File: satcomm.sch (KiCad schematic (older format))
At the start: 15 parts

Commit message: circuit extended
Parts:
- added C6: 10u TANT, symbol C
- added C7: 22u TANT, symbol C
- added R5: 121, symbol R
- added R6: 169, symbol R
- added U2: LM1117, symbol LM1117
- gave numbers to parts that had none: 15
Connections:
- net +5V: now also C6.1, U2.3 (VIN)
- net GND: now also C6.2, C7.2, R6.2
- new net +3V: C7.1, R5.1, R5.2, R6.1, U2.1 (ADJ/GND), U2.2 (VOUT)
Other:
- note added: "battery input / boost converter for 5V"
- note added: "linear voltage regulator for 3V\n"
- note added: "low pass / supercap buffer for 5V"
- moved on the sheet: BT1, C1, C2, C3, C4, C5, D1, L1, L2, R1, R2, R3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

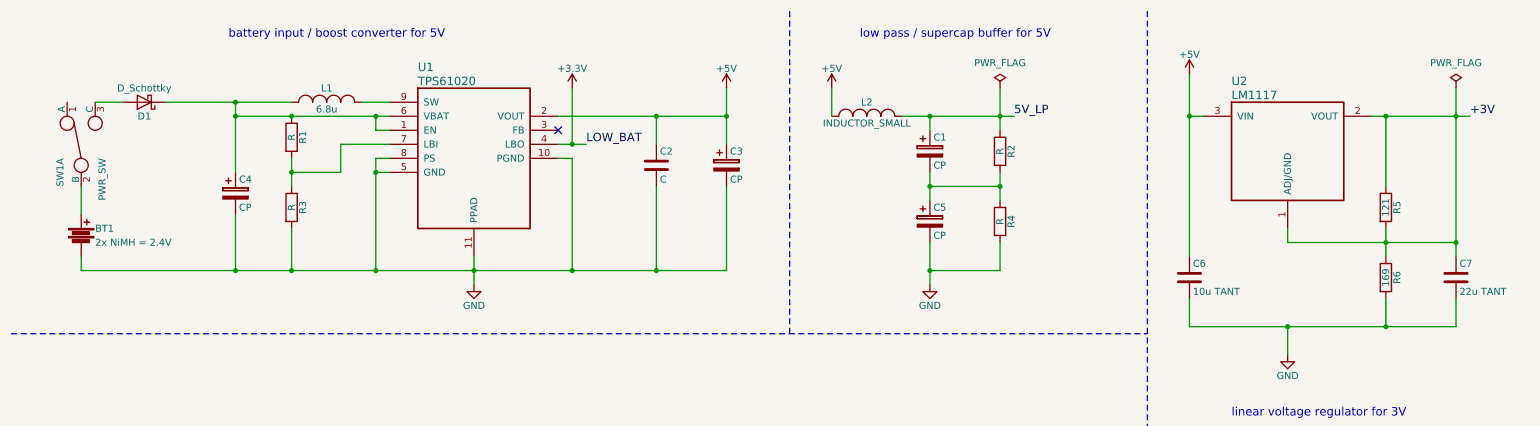
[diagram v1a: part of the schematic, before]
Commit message: added some zero ohm resistors for current measure
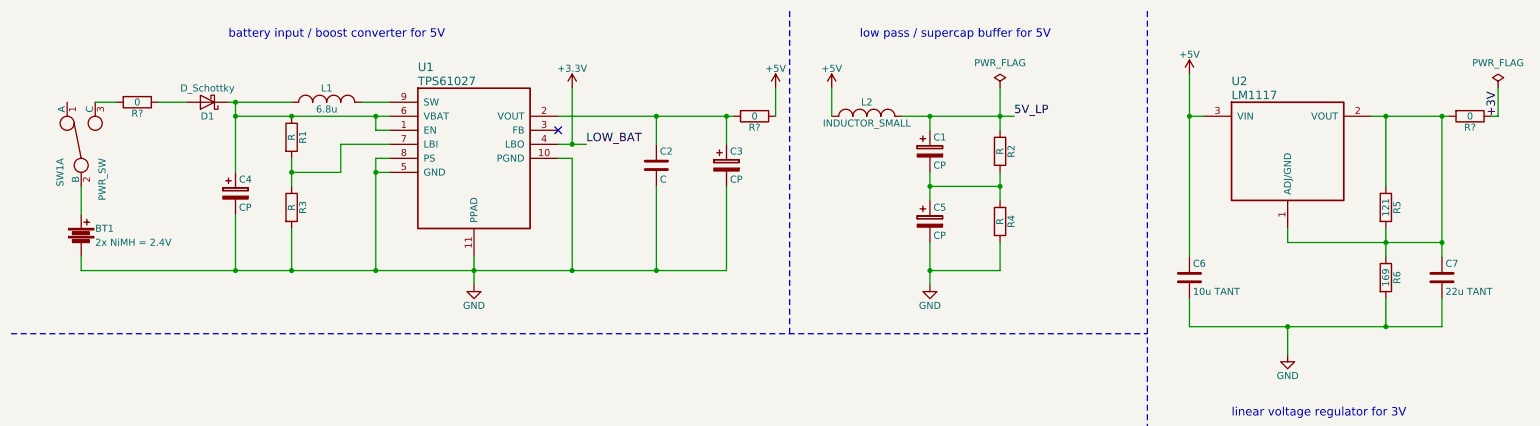
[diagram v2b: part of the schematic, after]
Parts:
- added R? (x3): 0, symbol R
- U1: value TPS61020 -> TPS61027
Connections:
- net +3V: now also R?.1; no longer C7.1, R5.1, R5.2, R6.1, U2.1 (ADJ/GND), U2.2 (VOUT)
- net +5V: now also R?.1; no longer C2.1, C3.1, U1.2 (VOUT)
- net at SW1.3 (C): now also R?.2; no longer D1.2 (A)
- new net: C2.1, C3.1, R?.2, U1.2 (VOUT)
- new net: D1.2 (A), R?.1
- new net: C7.1, R5.1, R5.2, R6.1, R?.2, U2.1 (ADJ/GND), U2.2 (VOUT)
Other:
- moved on the sheet: C7, D1
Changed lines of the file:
@@
 P 3150 1100
 F 0 "U1" H 3350 1350 60  0000 L CNN
-F 1 "TPS61020" H 3350 1250 60  0000 L CNN
+F 1 "TPS61027" H 3350 1250 60  0000 L CNN
 F 2 "" H 3150 1100 60  0000 C CNN
 F 3 "" H 3150 1100 60  0000 C CNN
@@
 	3150 1300 3050 1300
 Wire Wire Line
-	3050 1300 3050 1200
+	3050 1200 3050 1300
 Wire Wire Line
 	2050 1200 3150 1200
@@
 	2450 1500 2450 1700
 Wire Wire Line
-	2450 2000 2450 2300
+	2450 2300 2450 2000
 Connection ~ 3050 1200
 Connection ~ 3050 2300
@@
 L D_Schottky D1
 U 1 1 58D016A7
-P 1400 1100
-F 0 "D1" H 1400 1200 50  0000 C CNN
-F 1 "D_Schottky" H 1400 1000 50  0000 C CNN
-F 2 "" H 1400 1100 50  0000 C CNN
-F 3 "" H 1400 1100 50  0000 C CNN
-	1    1400 1100
+P 1850 1100
+F 0 "D1" H 1850 1200 50  0000 C CNN
+F 1 "D_Schottky" H 1850 1000 50  0000 C CNN
+F 2 "" H 1850 1100 50  0000 C CNN
+F 3 "" H 1850 1100 50  0000 C CNN
+	1    1850 1100
 	-1   0    0    1
 $EndComp
@@
 LOW_BAT
 Wire Wire Line
-	4350 1200 5550 1200
+	4350 1200 5600 1200
 Wire Wire Line
 	5050 1200 5050 1400
-Wire Wire Line
-	5550 1000 5550 1400
 Connection ~ 5050 1200
 Wire Wire Line
@@
 L +5V #PWR2
 U 1 1 58D035FF
-P 5550 1000
-F 0 "#PWR2" H 5550 850 50  0001 C CNN
-F 1 "+5V" H 5550 1140 50  0000 C CNN
-F 2 "" H 5550 1000 50  0000 C CNN
-F 3 "" H 5550 1000 50  0000 C CNN
-	1    5550 1000
+P 5900 1000
+F 0 "#PWR2" H 5900 850 50  0001 C CNN
+F 1 "+5V" H 5900 1140 50  0000 C CNN
+F 2 "" H 5900 1000 50  0000 C CNN
+F 3 "" H 5900 1000 50  0000 C CNN
+	1    5900 1000
 	1    0    0    -1
 $EndComp
@@
 L C C7
 U 1 1 58D0605E
-P 10750 2350
-F 0 "C7" H 10775 2450 50  0000 L CNN
-F 1 "22u TANT" H 10775 2250 50  0000 L CNN
-F 2 "" H 10788 2200 50  0000 C CNN
-F 3 "" H 10750 2350 50  0000 C CNN
-	1    10750 2350
+P 10650 2350
+F 0 "C7" H 10675 2450 50  0000 L CNN
+F 1 "22u TANT" H 10675 2250 50  0000 L CNN
+F 2 "" H 10688 2200 50  0000 C CNN
+F 3 "" H 10650 2350 50  0000 C CNN
+	1    10650 2350
 	1    0    0    -1
 $EndComp
@@
 $EndComp
 Wire Wire Line
-	10150 1200 10850 1200
+	10150 1200 10700 1200
 Wire Wire Line
 	10250 1200 10250 1700
@@
 	10250 2000 10250 2200
 Wire Wire Line
-	9550 2100 10750 2100
+	9550 2100 10650 2100
 Connection ~ 10250 2100
 Wire Wire Line
 	8850 2500 8850 2700
 Wire Wire Line
-	8850 2700 10750 2700
+	8850 2700 10650 2700
 Wire Wire Line
 	10250 2700 10250 2500
@@
 	8850 1200 8950 1200
 Wire Wire Line
-	10750 1000 10750 2200
-Connection ~ 10750 2100
+	10650 1200 10650 2200
 Connection ~ 10250 1200
 Wire Wire Line
-	10750 2700 10750 2500
+	10650 2700 10650 2500
 Connection ~ 10250 2700
 $Comp
@@
 L PWR_FLAG #FLG2
 U 1 1 58D06D13
-P 10750 1000
-F 0 "#FLG2" H 10750 1095 50  0001 C CNN
-F 1 "PWR_FLAG" H 10750 1180 50  0000 C CNN
-F 2 "" H 10750 1000 50  0000 C CNN
-F 3 "" H 10750 1000 50  0000 C CNN
-	1    10750 1000
-	1    0    0    -1
-$EndComp
-Connection ~ 10750 1200
-Text Label 10850 1200 0    60   ~ 0
-+3V
-Wire Wire Line
-	1550 1100 2450 1100
-Wire Wire Line
-	1250 1100 1050 1100
+P 11050 1000
+F 0 "#FLG2" H 11050 1095 50  0001 C CNN
+F 1 "PWR_FLAG" H 11050 1180 50  0000 C CNN
+F 2 "" H 11050 1000 50  0000 C CNN
+F 3 "" H 11050 1000 50  0000 C CNN
+	1    11050 1000
+	1    0    0    -1
+$EndComp
 Wire Wire Line
 	950  2300 5550 2300
 Wire Wire Line
-	9550 2000 9550 2100
+	9550 2100 9550 2000
 Wire Wire Line
 	9550 2700 9550 2900
@@
 Text Notes 2000 650  0    60   ~ 0
 battery input / boost converter for 5V
+Wire Wire Line
+	2000 1100 2450 1100
+$Comp
+L R R?
+U 1 1 58D08D36
+P 1350 1100
+F 0 "R?" V 1430 1100 50  0000 C CNN
+F 1 "0" V 1350 1100 50  0000 C CNN
+F 2 "" V 1280 1100 50  0000 C CNN
+F 3 "" H 1350 1100 50  0000 C CNN
+	1    1350 1100
+	0    1    1    0
+$EndComp
+Wire Wire Line
+	1700 1100 1500 1100
+Wire Wire Line
+	1200 1100 1050 1100
+$Comp
+L R R?
+U 1 1 58D08F6C
+P 5750 1200
+F 0 "R?" V 5830 1200 50  0000 C CNN
+F 1 "0" V 5750 1200 50  0000 C CNN
+F 2 "" V 5680 1200 50  0000 C CNN
+F 3 "" H 5750 1200 50  0000 C CNN
+	1    5750 1200
+	0    1    1    0
+$EndComp
+Wire Wire Line
+	5550 1400 5550 1200
+Wire Wire Line
+	5900 1200 5900 1000
+$Comp
+L R R?
+U 1 1 58D09272
+P 10850 1200
+F 0 "R?" V 10930 1200 50  0000 C CNN
+F 1 "0" V 10850 1200 50  0000 C CNN
+F 2 "" V 10780 1200 50  0000 C CNN
+F 3 "" H 10850 1200 50  0000 C CNN
+	1    10850 1200
+	0    1    1    0
+$EndComp
+Connection ~ 10650 2100
+Connection ~ 10650 1200
+Wire Wire Line
+	11000 1200 11050 1200
+Wire Wire Line
+	11050 1200 11050 1000
+Text Label 11050 1200 1    60   ~ 0
++3V
 $EndSCHEMATC

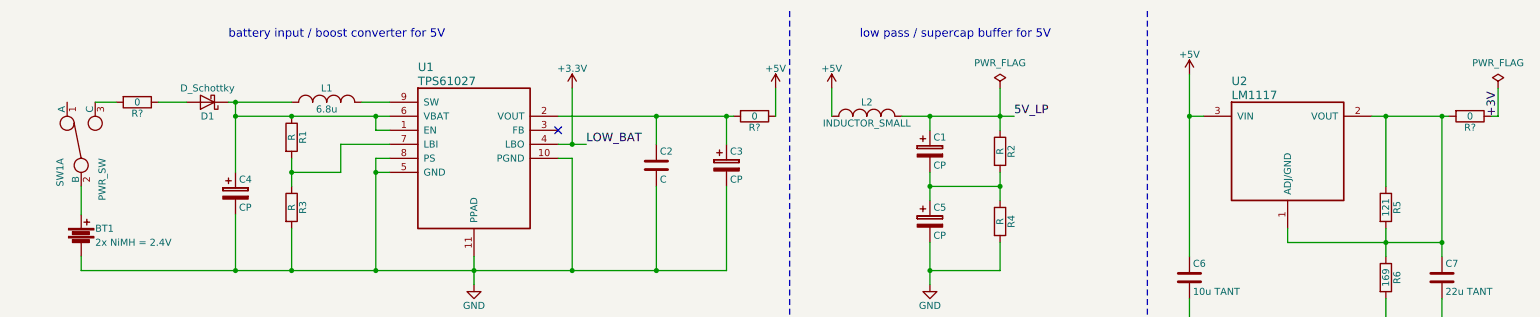
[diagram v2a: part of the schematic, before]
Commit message: added some footprint associations
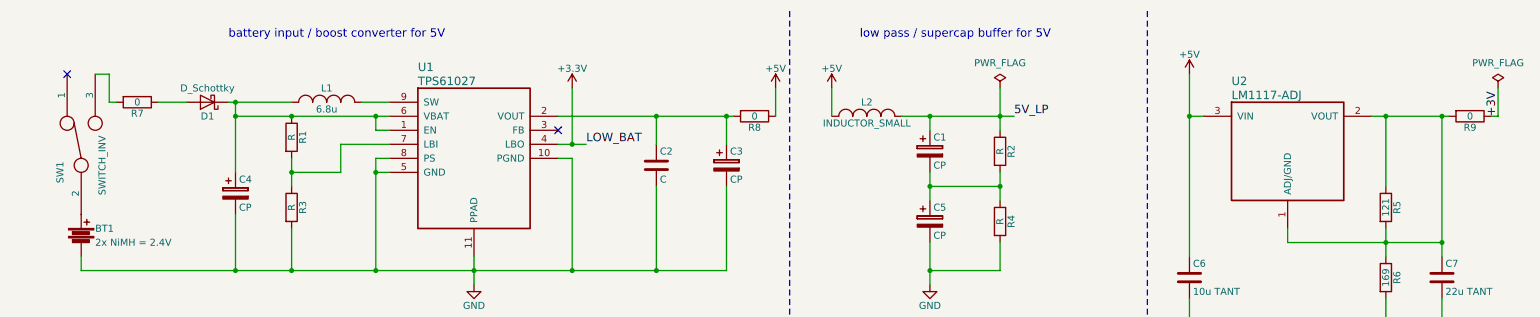
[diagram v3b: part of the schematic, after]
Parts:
- removed SW1: PWR_SW, symbol Switch_SPDT_x2
- added SW1: SWITCH_INV, Morn_Mechanical:EG1218, symbol SWITCH_INV
- U1: footprint (none) -> Morn_SMD_NoLeads:S-PVSON-N10
- U2: value LM1117 -> LM1117-ADJ; footprint (none) -> TO_SOT_Packages_SMD:TO-252-2Lead
- gave numbers to parts that had none: 3
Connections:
- net at BT1.1: now also SW1.2
- net at R7.2: now also SW1.3
- no-connect marks 1 -> 2
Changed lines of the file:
@@
 LIBS:contrib
 LIBS:valves
-LIBS:tsp61027
-LIBS:lm1117
+LIBS:MornsPMIC
 LIBS:satcomm-cache
 EELAYER 25 0
@@
 F 0 "BT1" H 1050 2100 50  0000 L CNN
 F 1 "2x NiMH = 2.4V" H 1050 2000 50  0000 L CNN
-F 2 "" V 950 2090 50  0000 C CNN
+F 2 "" V 950 2090 50  0001 C CNN
 F 3 "" V 950 2090 50  0000 C CNN
 	1    950  2050
@@
 $EndComp
 $Comp
-L Switch_SPDT_x2 SW1
-U 1 1 58D0088A
-P 950 1400
-F 0 "SW1" H 750 1550 50  0000 C CNN
-F 1 "PWR_SW" H 700 1250 50  0000 C CNN
-F 2 "" H 950 1400 50  0000 C CNN
-F 3 "" H 950 1400 50  0000 C CNN
-	1    950  1400
-	0    -1   -1   0
-$EndComp
-$Comp
-L GND #PWR5
+L GND #PWR01
 U 1 1 58D0108E
 P 3750 2400
-F 0 "#PWR5" H 3750 2150 50  0001 C CNN
+F 0 "#PWR01" H 3750 2150 50  0001 C CNN
 F 1 "GND" H 3750 2250 50  0000 C CNN
 F 2 "" H 3750 2400 50  0000 C CNN
@@
 	1    0    0    -1
 $EndComp
-$Comp
-L TPS61020 U1
-U 1 1 58D01179
-P 3150 1100
-F 0 "U1" H 3350 1350 60  0000 L CNN
-F 1 "TPS61027" H 3350 1250 60  0000 L CNN
-F 2 "" H 3150 1100 60  0000 C CNN
-F 3 "" H 3150 1100 60  0000 C CNN
-	1    3150 1100
-	1    0    0    -1
-$EndComp
 Wire Wire Line
 	3150 1600 3050 1600
@@
 	3150 1300 3050 1300
 Wire Wire Line
-	3050 1200 3050 1300
+	3050 1300 3050 1200
 Wire Wire Line
 	2050 1200 3150 1200
@@
 F 0 "R1" V 2530 1350 50  0000 C CNN
 F 1 "R" V 2450 1350 50  0000 C CNN
-F 2 "" V 2380 1350 50  0000 C CNN
+F 2 "" V 2380 1350 50  0001 C CNN
 F 3 "" H 2450 1350 50  0000 C CNN
 	1    2450 1350
@@
 F 0 "R3" V 2530 1850 50  0000 C CNN
 F 1 "R" V 2450 1850 50  0000 C CNN
-F 2 "" V 2380 1850 50  0000 C CNN
+F 2 "" V 2380 1850 50  0001 C CNN
 F 3 "" H 2450 1850 50  0000 C CNN
 	1    2450 1850
@@
 F 0 "L1" H 2700 1200 50  0000 C CNN
 F 1 "6.8u" H 2700 1050 50  0000 C CNN
-F 2 "" H 2700 1100 50  0000 C CNN
+F 2 "" H 2700 1100 50  0001 C CNN
 F 3 "" H 2700 1100 50  0000 C CNN
 	1    2700 1100
@@
 F 0 "D1" H 1850 1200 50  0000 C CNN
 F 1 "D_Schottky" H 1850 1000 50  0000 C CNN
-F 2 "" H 1850 1100 50  0000 C CNN
+F 2 "" H 1850 1100 50  0001 C CNN
 F 3 "" H 1850 1100 50  0000 C CNN
 	1    1850 1100
@@
 F 0 "C4" H 2075 1850 50  0000 L CNN
 F 1 "CP" H 2075 1650 50  0000 L CNN
-F 2 "" H 2088 1600 50  0000 C CNN
+F 2 "" H 2088 1600 50  0001 C CNN
 F 3 "" H 2050 1750 50  0000 C CNN
 	1    2050 1750
@@
 	2050 1900 2050 2300
 Connection ~ 2050 2300
-Wire Wire Line
-	950  1700 950  1900
 Wire Wire Line
 	950  2200 950  2300
@@
 F 0 "C2" H 5075 1650 50  0000 L CNN
 F 1 "C" H 5075 1450 50  0000 L CNN
-F 2 "" H 5088 1400 50  0000 C CNN
+F 2 "" H 5088 1400 50  0001 C CNN
 F 3 "" H 5050 1550 50  0000 C CNN
 	1    5050 1550
@@
 F 0 "C3" H 5575 1650 50  0000 L CNN
 F 1 "CP" H 5575 1450 50  0000 L CNN
-F 2 "" H 5588 1400 50  0000 C CNN
+F 2 "" H 5588 1400 50  0001 C CNN
 F 3 "" H 5550 1550 50  0000 C CNN
 	1    5550 1550
@@
 NoConn ~ 4350 1300
 $Comp
-L +5V #PWR2
+L +5V #PWR02
 U 1 1 58D035FF
 P 5900 1000
-F 0 "#PWR2" H 5900 850 50  0001 C CNN
+F 0 "#PWR02" H 5900 850 50  0001 C CNN
 F 1 "+5V" H 5900 1140 50  0000 C CNN
 F 2 "" H 5900 1000 50  0000 C CNN
@@
 Connection ~ 5550 1200
 $Comp
-L +3.3V #PWR1
+L +3.3V #PWR03
 U 1 1 58D03676
 P 4450 1000
-F 0 "#PWR1" H 4450 850 50  0001 C CNN
+F 0 "#PWR03" H 4450 850 50  0001 C CNN
 F 1 "+3.3V" H 4450 1140 50  0000 C CNN
 F 2 "" H 4450 1000 50  0000 C CNN
@@
 F 0 "C1" H 7025 1550 50  0000 L CNN
 F 1 "CP" H 7025 1350 50  0000 L CNN
-F 2 "" H 7038 1300 50  0000 C CNN
+F 2 "" H 7038 1300 50  0001 C CNN
 F 3 "" H 7000 1450 50  0000 C CNN
 	1    7000 1450
@@
 F 0 "C5" H 7025 2050 50  0000 L CNN
 F 1 "CP" H 7025 1850 50  0000 L CNN
-F 2 "" H 7038 1800 50  0000 C CNN
+F 2 "" H 7038 1800 50  0001 C CNN
 F 3 "" H 7000 1950 50  0000 C CNN
 	1    7000 1950
@@
 F 0 "R2" V 7580 1450 50  0000 C CNN
 F 1 "R" V 7500 1450 50  0000 C CNN
-F 2 "" V 7430 1450 50  0000 C CNN
+F 2 "" V 7430 1450 50  0001 C CNN
 F 3 "" H 7500 1450 50  0000 C CNN
 	1    7500 1450
@@
 F 0 "R4" V 7580 1950 50  0000 C CNN
 F 1 "R" V 7500 1950 50  0000 C CNN
-F 2 "" V 7430 1950 50  0000 C CNN
+F 2 "" V 7430 1950 50  0001 C CNN
 F 3 "" H 7500 1950 50  0000 C CNN
 	1    7500 1950
@@
 	7000 2100 7000 2400
 $Comp
-L GND #PWR6
+L GND #PWR04
 U 1 1 58D039CB
 P 7000 2400
-F 0 "#PWR6" H 7000 2150 50  0001 C CNN
+F 0 "#PWR04" H 7000 2150 50  0001 C CNN
 F 1 "GND" H 7000 2250 50  0000 C CNN
 F 2 "" H 7000 2400 50  0000 C CNN
@@
 F 0 "L2" H 6550 1300 50  0000 C CNN
 F 1 "INDUCTOR_SMALL" H 6550 1150 50  0000 C CNN
-F 2 "" H 6550 1200 50  0000 C CNN
+F 2 "" H 6550 1200 50  0001 C CNN
 F 3 "" H 6550 1200 50  0000 C CNN
 	1    6550 1200
@@
 	6300 1200 6300 1000
 $Comp
-L +5V #PWR3
+L +5V #PWR05
 U 1 1 58D03B2B
 P 6300 1000
-F 0 "#PWR3" H 6300 850 50  0001 C CNN
+F 0 "#PWR05" H 6300 850 50  0001 C CNN
 F 1 "+5V" H 6300 1140 50  0000 C CNN
 F 2 "" H 6300 1000 50  0000 C CNN
@@
 Text Label 7600 1200 0    60   ~ 0
 5V_LP
-$Comp
-L LM1117 U2
-U 1 1 58D05F36
-P 8950 1200
-F 0 "U2" H 9150 1450 60  0000 L CNN
-F 1 "LM1117" H 9150 1350 60  0000 L CNN
-F 2 "" H 8950 1200 60  0000 C CNN
-F 3 "" H 8950 1200 60  0000 C CNN
-	1    8950 1200
-	1    0    0    -1
-$EndComp
 $Comp
 L C C7
@@
 F 0 "C7" H 10675 2450 50  0000 L CNN
 F 1 "22u TANT" H 10675 2250 50  0000 L CNN
-F 2 "" H 10688 2200 50  0000 C CNN
+F 2 "" H 10688 2200 50  0001 C CNN
 F 3 "" H 10650 2350 50  0000 C CNN
 	1    10650 2350
@@
 F 0 "C6" H 8875 2450 50  0000 L CNN
 F 1 "10u TANT" H 8875 2250 50  0000 L CNN
-F 2 "" H 8888 2200 50  0000 C CNN
+F 2 "" H 8888 2200 50  0001 C CNN
 F 3 "" H 8850 2350 50  0000 C CNN
 	1    8850 2350
@@
 F 0 "R6" V 10330 2350 50  0000 C CNN
 F 1 "169" V 10250 2350 50  0000 C CNN
-F 2 "" V 10180 2350 50  0000 C CNN
+F 2 "" V 10180 2350 50  0001 C CNN
 F 3 "" H 10250 2350 50  0000 C CNN
 	1    10250 2350
@@
 F 0 "R5" V 10330 1850 50  0000 C CNN
 F 1 "121" V 10250 1850 50  0000 C CNN
-F 2 "" V 10180 1850 50  0000 C CNN
+F 2 "" V 10180 1850 50  0001 C CNN
 F 3 "" H 10250 1850 50  0000 C CNN
 	1    10250 1850
@@
 Connection ~ 10250 2700
 $Comp
-L GND #PWR7
+L GND #PWR06
 U 1 1 58D06A4B
 P 9550 2900
-F 0 "#PWR7" H 9550 2650 50  0001 C CNN
+F 0 "#PWR06" H 9550 2650 50  0001 C CNN
 F 1 "GND" H 9550 2750 50  0000 C CNN
 F 2 "" H 9550 2900 50  0000 C CNN
@@
 $EndComp
 $Comp
-L +5V #PWR4
+L +5V #PWR07
 U 1 1 58D06AEE
 P 8850 900
-F 0 "#PWR4" H 8850 750 50  0001 C CNN
+F 0 "#PWR07" H 8850 750 50  0001 C CNN
 F 1 "+5V" H 8850 1040 50  0000 C CNN
 F 2 "" H 8850 900 50  0000 C CNN
@@
 Connection ~ 8850 1200
 $Comp
-L PWR_FLAG #FLG1
+L PWR_FLAG #FLG08
 U 1 1 58D06B92
 P 7500 1000
-F 0 "#FLG1" H 7500 1095 50  0001 C CNN
+F 0 "#FLG08" H 7500 1095 50  0001 C CNN
 F 1 "PWR_FLAG" H 7500 1180 50  0000 C CNN
 F 2 "" H 7500 1000 50  0000 C CNN
@@
 $EndComp
 $Comp
-L PWR_FLAG #FLG2
+L PWR_FLAG #FLG09
 U 1 1 58D06D13
 P 11050 1000
-F 0 "#FLG2" H 11050 1095 50  0001 C CNN
+F 0 "#FLG09" H 11050 1095 50  0001 C CNN
 F 1 "PWR_FLAG" H 11050 1180 50  0000 C CNN
 F 2 "" H 11050 1000 50  0000 C CNN
@@
 	2000 1100 2450 1100
 $Comp
-L R R?
+L R R7
 U 1 1 58D08D36
 P 1350 1100
-F 0 "R?" V 1430 1100 50  0000 C CNN
+F 0 "R7" V 1430 1100 50  0000 C CNN
 F 1 "0" V 1350 1100 50  0000 C CNN
-F 2 "" V 1280 1100 50  0000 C CNN
+F 2 "" V 1280 1100 50  0001 C CNN
 F 3 "" H 1350 1100 50  0000 C CNN
 	1    1350 1100
@@
 Wire Wire Line
 	1700 1100 1500 1100
-Wire Wire Line
-	1200 1100 1050 1100
-$Comp
-L R R?
+$Comp
+L R R8
 U 1 1 58D08F6C
 P 5750 1200
-F 0 "R?" V 5830 1200 50  0000 C CNN
+F 0 "R8" V 5830 1200 50  0000 C CNN
 F 1 "0" V 5750 1200 50  0000 C CNN
-F 2 "" V 5680 1200 50  0000 C CNN
+F 2 "" V 5680 1200 50  0001 C CNN
 F 3 "" H 5750 1200 50  0000 C CNN
 	1    5750 1200
@@
 	5900 1200 5900 1000
 $Comp
-L R R?
+L R R9
 U 1 1 58D09272
 P 10850 1200
-F 0 "R?" V 10930 1200 50  0000 C CNN
+F 0 "R9" V 10930 1200 50  0000 C CNN
 F 1 "0" V 10850 1200 50  0000 C CNN
-F 2 "" V 10780 1200 50  0000 C CNN
+F 2 "" V 10780 1200 50  0001 C CNN
 F 3 "" H 10850 1200 50  0000 C CNN
 	1    10850 1200
@@
 Text Label 11050 1200 1    60   ~ 0
 +3V
+$Comp
+L TPS61020 U1
+U 1 1 58D11957
+P 3150 1100
+F 0 "U1" H 3350 1350 60  0000 L CNN
+F 1 "TPS61027" H 3350 1250 60  0000 L CNN
+F 2 "Morn_SMD_NoLeads:S-PVSON-N10" H 3150 1100 60  0001 C CNN
+F 3 "" H 3150 1100 60  0000 C CNN
+	1    3150 1100
+	1    0    0    -1
+$EndComp
+$Comp
+L LM1117 U2
+U 1 1 58D11A1B
+P 8950 1200
+F 0 "U2" H 9150 1450 60  0000 L CNN
+F 1 "LM1117-ADJ" H 9150 1350 60  0000 L CNN
+F 2 "TO_SOT_Packages_SMD:TO-252-2Lead" H 8950 1200 60  0001 C CNN
+F 3 "" H 8950 1200 60  0000 C CNN
+	1    8950 1200
+	1    0    0    -1
+$EndComp
+$Comp
+L SWITCH_INV SW1
+U 1 1 58D2FB6C
+P 950 1400
+F 0 "SW1" H 750 1550 50  0000 C CNN
+F 1 "SWITCH_INV" H 800 1250 50  0000 C CNN
+F 2 "Morn_Mechanical:EG1218" H 950 1400 50  0001 C CNN
+F 3 "" H 950 1400 50  0000 C CNN
+	1    950  1400
+	0    -1   -1   0
+$EndComp
+Wire Wire Line
+	1050 900  1150 900
+Wire Wire Line
+	1150 900  1150 1100
+Wire Wire Line
+	1150 1100 1200 1100
+NoConn ~ 850  900
 $EndSCHEMATC

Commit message: added stm32 uc
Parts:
- added C? (x4): 100n, symbol C
- added C?: 1u, symbol C
- added C?: 4u7, symbol C
- added J?: CONN_02X10, symbol CONN_02X10
- added R? (x3): DNP, symbol R
- added U?: STM32F411xC/xE, symbol STM32F411xC/xE
- BT1: symbol Battery -> Battery-RESCUE-satcomm
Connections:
- net +3V: now also C?.1, C?.2, C?.2, C?.2, C?.2, J?.1 (P1), J?.2 (P2), R?.1, R?.1, U?.1 (VBAT), U?.24 (VDD), U?.36 (VDD), U?.48 (VDD), U?.9 (VDDA_VREF+)
- net GND: now also C?.1, C?.1, C?.1, C?.1, C?.2, C?.2, J?.10 (P10), J?.12 (P12), J?.14 (P14), J?.16 (P16), J?.18 (P18), J?.20 (P20), J?.4 (P4), J?.6 (P6), J?.8 (P8), R?.2, U?.23 (VSS), U?.35 (VSS), U?.47 (VSS), U?.8 (VSSA_VREF-)
- new net: C?.1, U?.22 (VCAP_1)
- new net BOOT0: R?.1, R?.2, U?.44 (BOOT0)
- new net RESET: J?.15 (P15), R?.2, U?.7 (NRST)
- new net TCK: J?.9 (P9), U?.37 (PA14)
- new net TDI: J?.5 (P5), U?.38 (PA15)
- new net TDO: J?.13 (P13), U?.39 (PB3)
- new net TMS: J?.7 (P7), U?.34 (PA13)
- new net nTRST: J?.3 (P3), U?.40 (PB4)
- no-connect marks 2 -> 5
